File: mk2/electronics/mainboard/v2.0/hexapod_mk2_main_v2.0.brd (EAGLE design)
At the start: 84.5 x 61 mm, 22 parts, among them U1 74LVC1T45GW,125TSSOP6_SOT363-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

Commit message: fix board sever
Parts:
- removed BUCK_IN, BUCK_OUT: XT30PW-M, amass:XT30PW-M
- removed S1: SWS004, smd-special:SMS-004
- removed U1: 74LVC1T45GW,125TSSOP6_SOT363-2_NEX-M, logic-level-converter:TSSOP6_SOT363-2_NEX-M
- added DFR0753: DFR0753, DFR0753:DFR0753
- added FUSE_HOLDER: 3555-2, 3555-2:FUSE_3555-2
- added U2: SN74LVC1T45DBVR, SN74LVC1T45DBVR:SOT95P280X145-6N
- E_STOP: value XT30PW-M -> XT60PW-M; device amass:XT30PW-M -> amass:XT60PW-M
- moved E_STOP 38.1 mm to (-13.2, -21.6), turned to 0 degrees
- renumbered 12V to 2S, 1KΩ to 680Ω
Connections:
- removed net 12V: 2S.A, BUCK_IN.+, E_STOP.-, R1.2
- removed net 12V_PRE: BATTERY.+, E_STOP.+
- removed net D_SW0: RPI5.22, S1.1
- removed net D_SW1: RPI5.24, S1.2
- removed net D_SW2: RPI5.26, S1.3
- removed net D_SW3: RPI5.28, S1.4
- new net 2S_BAT: BATTERY.+, E_STOP.-
- new net 2S_ESTOP: E_STOP.+, FUSE_HOLDER.1_1, FUSE_HOLDER.1_2
- new net 2S_PROT: 2S.A, DFR0753.VIN, FUSE_HOLDER.2_1, FUSE_HOLDER.2_2, LEG0.P$3, LEG1.P$3, LEG2.P$3, LEG3.P$3, LEG4.P$3, LEG5.P$3, R1.2
- net 3.3V: now also U2.6; no longer P_BUTTON.1, S1.5, S1.6, S1.7, S1.8, U1.6
- net 5V: now also DFR0753.VOUT, U2.1; no longer BUCK_OUT.+, LEG0.P$3, LEG1.P$3, LEG2.P$3, LEG3.P$3, LEG4.P$3, LEG5.P$3, U1.1
- net GND: now also DFR0753.GND, P_BUTTON.1, U2.2, U2.5; no longer BUCK_IN.-, BUCK_OUT.-, U1.2, U1.5
- net LEDSIG: now also RPI5.19, U2.4; no longer RPI5.33, U1.4
- net LEDSIG_CONV: now also U2.3; no longer U1.3
- net PWRSIG: now also RPI5.11; no longer RPI5.3, U$1.0-RX1/CS1/CRX2
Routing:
- net LEDSIG: track 73.9 -> 0.00 mm
- net PWRSIG: track 123.9 -> 60.6 mm
- net 12V: track 61.5 -> 0.00 mm, vias 1 -> 0
- net 3.3V: track 110.2 -> 68.2 mm, vias 3 -> 2
- net D_SW3: track 37.8 -> 0.00 mm
- net 2S_PROT: track 0.00 -> 36.1 mm, vias 0 -> 1
- net D_SW0: track 33.4 -> 0.00 mm, vias 1 -> 0
- net D_SW2: track 33.3 -> 0.00 mm, vias 1 -> 0
- net D_SW1: track 31.7 -> 0.00 mm, vias 1 -> 0
- net 12V_PRE: track 25.0 -> 0.00 mm
- net GND: track 50.6 -> 60.5 mm
- net 5V: track 30.4 -> 33.2 mm
- net LEDSIG_CONV: track 29.3 -> 31.6 mm

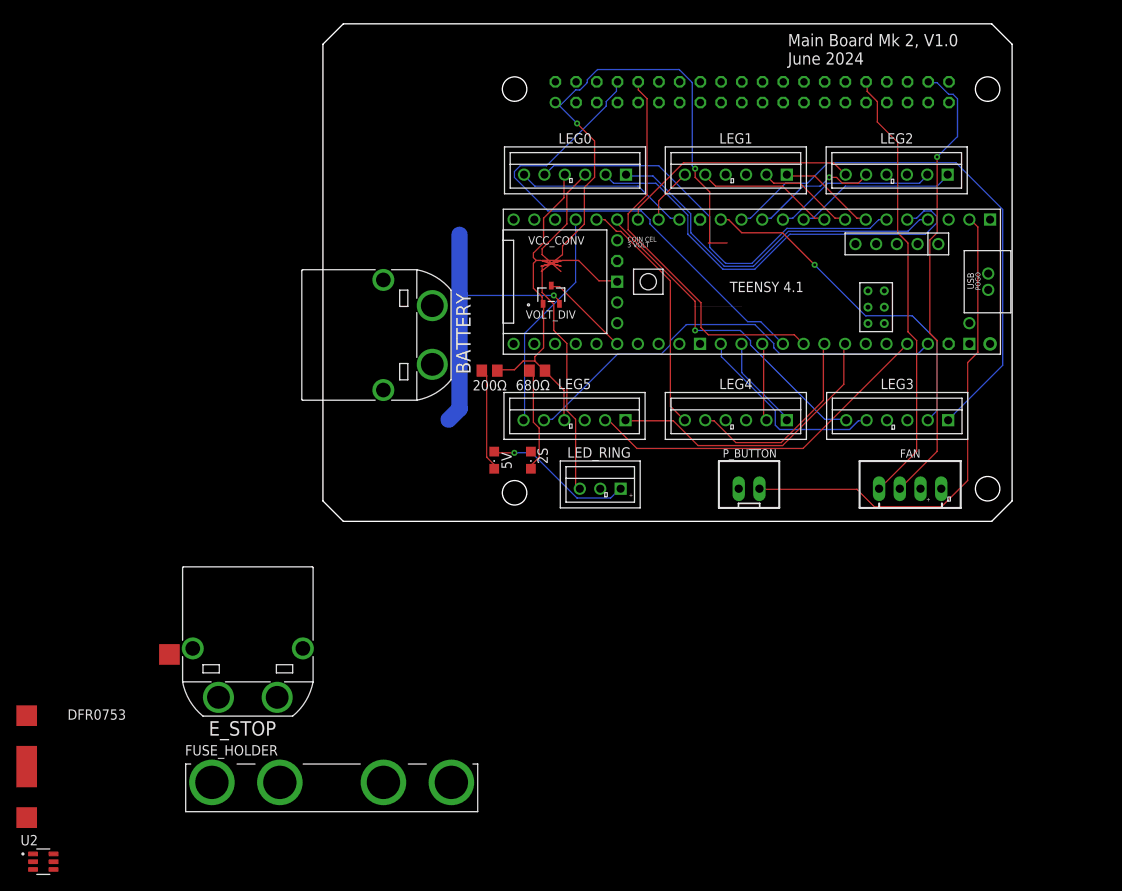
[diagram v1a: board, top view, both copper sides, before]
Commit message: pcb board layout
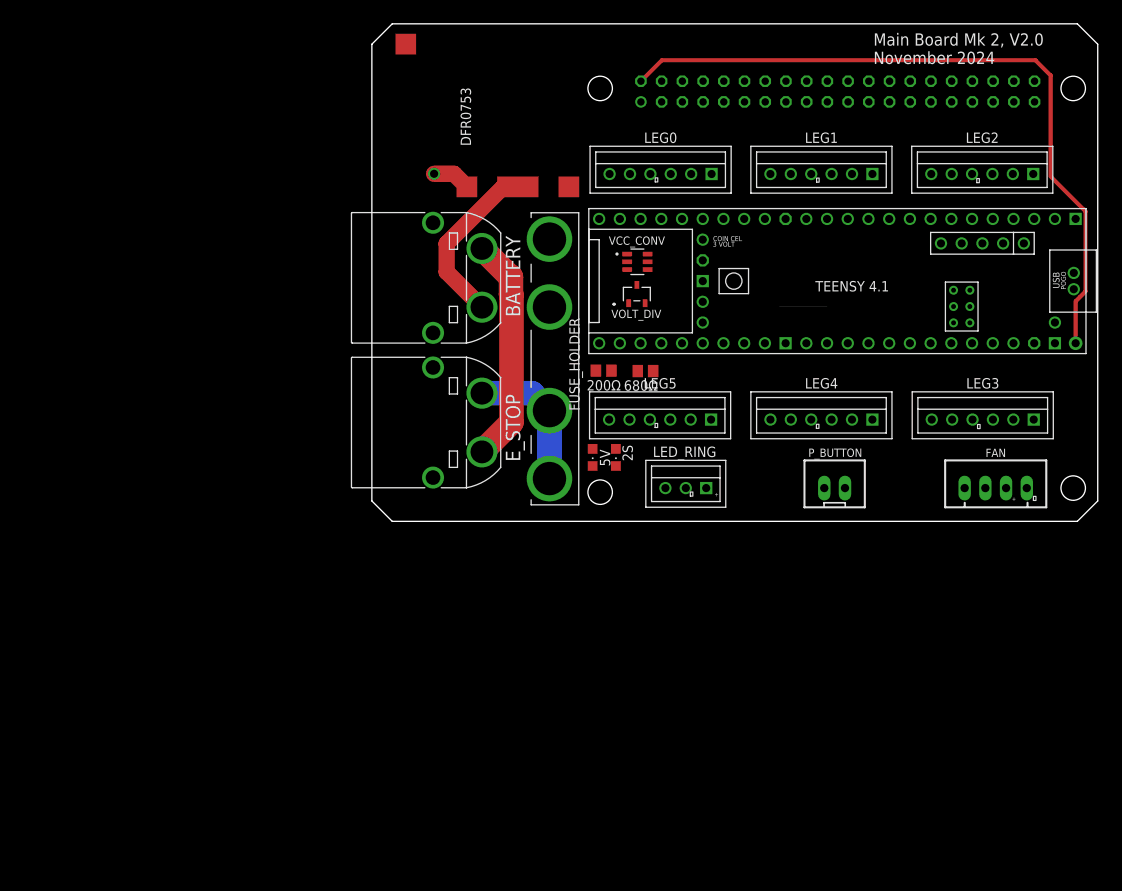
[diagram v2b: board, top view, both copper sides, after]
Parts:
- moved U2 103.5 mm to (34.6, 31.8)
- moved DFR0753 89.7 mm to (16.2, 49.5), turned to 90 degrees
- moved FUSE_HOLDER 58.4 mm to (23.8, 19.9), turned to 90 degrees
- moved E_STOP 44.3 mm to (15.5, 12.1), turned to 90 degrees
- moved 200Ω 14.0 mm to (30.4, 18.5)
- moved 680Ω 13.3 mm to (35.5, 18.4)
- moved 5V 12.1 mm to (29.1, 7.84)
- moved LEG0 10.5 mm to (37.4, 42.6)
- moved FAN 10.5 mm to (78.5, 4.08)
- moved LED_RING 10.5 mm to (40.5, 4.08)
- moved LEG1 10.5 mm to (57.1, 42.6)
- moved LEG2 10.5 mm to (76.8, 42.6)
- moved LEG3 10.5 mm to (76.9, 12.5)
- moved LEG4 10.5 mm to (57.1, 12.5)
- moved LEG5 10.5 mm to (37.3, 12.5)
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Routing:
- net 3.3V: track 68.2 -> 0.00 mm, vias 2 -> 0
- net L3M1: track 65.9 -> 0.00 mm
- net PWRSIG: track 60.6 -> 0.00 mm
- net RPI_TX: track 60.5 -> 0.00 mm
- net 5V: track 33.2 -> 91.9 mm
- net FAN_RPM: track 56.0 -> 0.00 mm, vias 1 -> 0
- net L5M3: track 54.5 -> 0.00 mm
- net FAN_PWM: track 54.4 -> 0.00 mm
- net L0M2: track 54.4 -> 0.00 mm
- net L0M3: track 51.8 -> 0.00 mm
- net RPI_RX: track 48.6 -> 0.00 mm
- net L0M1: track 45.4 -> 0.00 mm
- net L5M2: track 43.8 -> 0.00 mm
- net L3M2: track 42.9 -> 0.00 mm, vias 1 -> 0
- net L3SIG: track 41.0 -> 0.00 mm, vias 1 -> 0
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- added copper zone on layer 2, net 2S_PROT
- added copper zone on layer 2, net 5V
- added copper zone on layer 15, net GND
- removed copper zone on layer 15, net 5V
- removed copper zone on layer 2, net GND
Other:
- board size 84.5 x 61 mm -> 89 x 61 mm
- board text added: "Main Board Mk 2, V2.0 November 2024"
- board text removed: "Main Board Mk 2, V1.0 June 2024"
